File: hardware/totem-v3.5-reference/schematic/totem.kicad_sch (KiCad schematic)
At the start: 30 parts, among them J1 USB_C_Receptacle_USB2.0_16P, J2 LiPo 1000mAh, J3 u.FL GNSS, Q1 LED supply switch, SW1 power, SW2 SOS, U1 ESP32-WROOM-32E, U2 MAX-M10S, U4 AP2127K-3.3, U5 ICM-20948

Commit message: feat: footprints the library already knew, a title block, and the root sheet instance
Three things the documentation says a schematic should carry and this one
did not.

Footprints. Every one of the 85 placed instances had an empty Footprint
field — "each symbol in the schematic needs to have a footprint assigned to
it during the schematic entry process" (getting_started_in_kicad). Several
library symbols already name the package they are normally fitted in, and
that was being read and thrown away: the ESP32 module, the MAX-M10S, the
SOT-23-5 regulator, the ICM-20948's QFN and the WS2812B all arrive with one.
Eleven instances now carry a real footprint instead of a blank. The rest are
passives, connectors and switches, where the library cannot know and a
person has to choose.

A title block, which was empty. A sheet that says nothing about what it is
or how far to trust it is no good to anyone, and this one has to say both:
that it is a reconstruction rather than the Totem's recovered circuit, that
the passive values are designed to satisfy the firmware, that it is
generated and the source is what to edit, and that U3 is absent from the
drawing because no KiCad symbol for a TP4056 exists.

The root sheet_instances section, which the file format documentation lists
as a section of its own and which was simply missing.

Claude-Session: https://claude.ai/code/session_0192KwQN6XkBBxwoQn8x3FMV
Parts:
- DS1, DS61: footprint (none) -> LED_SMD:LED_WS2812B_PLCC4_5.0x5.0mm_P3.2mm
- U1: footprint (none) -> RF_Module:ESP32-WROOM-32E
- U2: footprint (none) -> RF_GPS:ublox_MAX
- U4: footprint (none) -> Package_TO_SOT_SMD:SOT-23-5
- U5: footprint (none) -> Sensor_Motion:InvenSense_QFN-24_3x3mm_P0.4mm
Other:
- company: (none) -> reconstruction, not the Totem's recovered circuit
- title: (none) -> Totem v3.5 — reference design

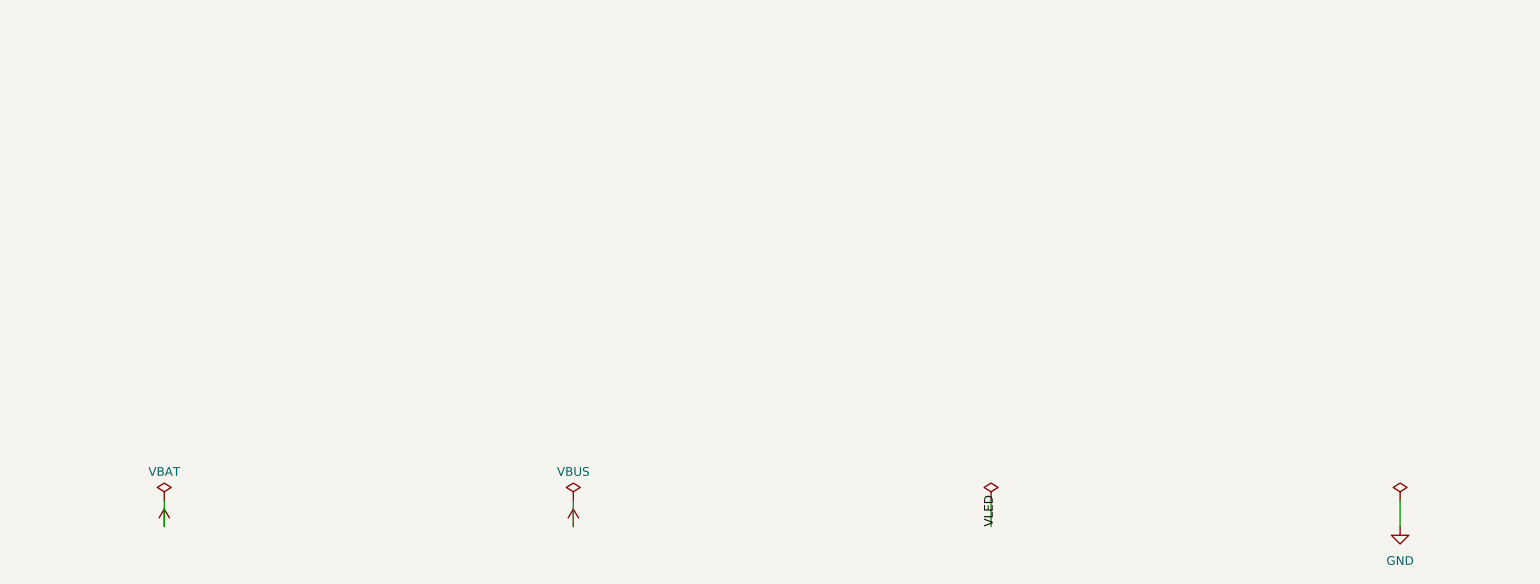
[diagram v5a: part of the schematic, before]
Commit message: fix: the charger was wired wrong, and the sheet was hiding it
I wrote "no KiCad symbol exists for the TP4056" and declared the part by
hand. Both halves were wrong. Battery_Management:TP4056-42-ESOP8 is in the
stock library, and the pinout I invented does not match the real part:

  pin 6  I called BAT2, "same die node as 5", and wired it to VBAT.
         It is STDBY, an open-drain status output.
  pin 8  I called STDBY and left it open.
         It is CE, the chip enable, and it is active high.

So the reference design shorted an open-drain output to the battery rail,
and never enabled the charger at all — CE floating means the part does
nothing. It would not have charged. Pin 6 is open now, CE is tied to the
input supply so charging runs whenever the cable is in, and pin 9, the
exposed thermal pad, goes to ground.

That the part was hand-declared is also why it was missing from the
drawing: a SKiDL-only part has no library, so it fell into `undrawn` and
the sheet quietly showed 30 of 31 components. The generator's own docstring
claimed it "cannot drift from the netlist"; this was the path that
falsified it. The sheet now has 31 symbols and the claim is true again.

Two things followed on their own. The VBAT PWR_FLAG is gone: the charger's
BAT pin is a real power output, so the rail has a genuine driver, and the
flag had been standing in for the missing part — quiet compensation that
hid the hole instead of showing it. And SKiDL's ERC went from two warnings
to none, so check.py's allowlist is empty, which is the honest state.

Verified by round trip, which is new and which would have caught this on
its own: KiCad exports a netlist back out of the drawing, and it now
carries the same 31 references as the netlist the circuit was built from,
with nothing on either side that is not on the other.

Claude-Session: https://claude.ai/code/session_0192KwQN6XkBBxwoQn8x3FMV
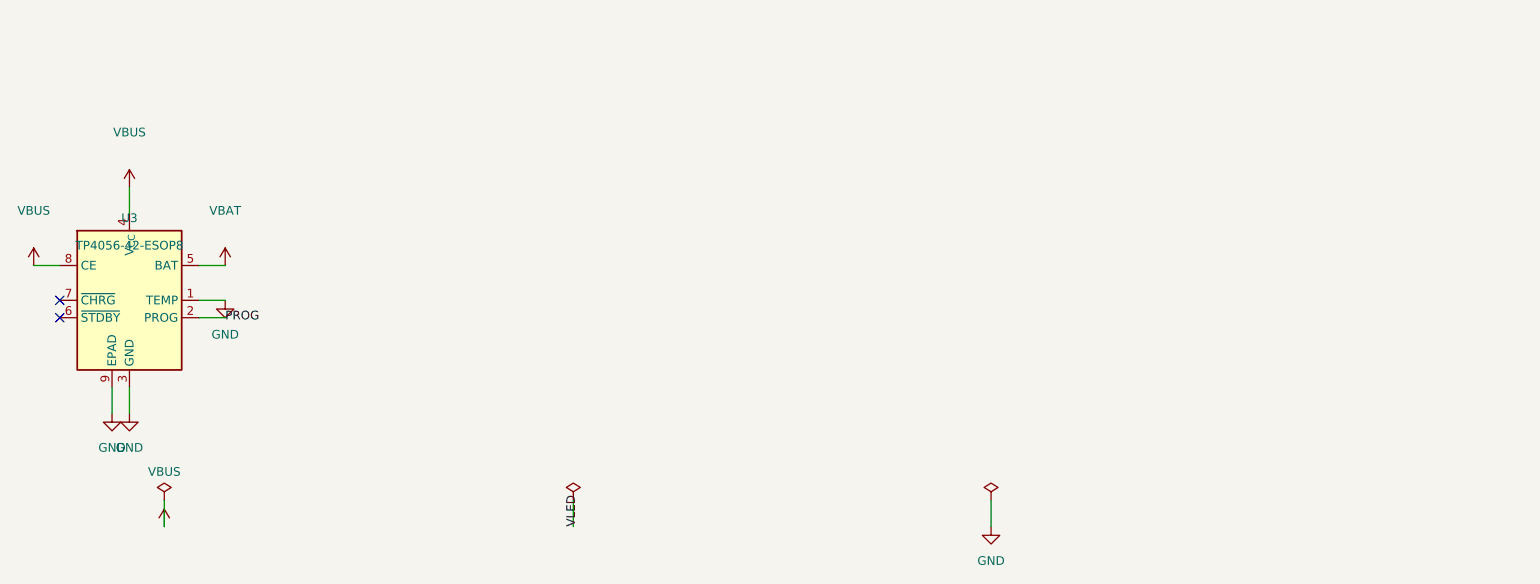
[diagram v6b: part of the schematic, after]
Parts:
- added U3: TP4056-42-ESOP8, Package_SO:SOIC-8-1EP_3.9x4.9mm_P1.27mm_EP2.41x3.3mm_ThermalVias, symbol Battery_Management:TP4056-42-ESOP8
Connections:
- net GND: now also U3.1 (TEMP), U3.3 (GND), U3.9 (EPAD)
- net PROG: now also U3.2 (PROG)
- net VBAT: now also U3.5 (BAT)
- net VBUS: now also U3.4 (V_{CC}), U3.8 (CE)
- no-connect marks 54 -> 56

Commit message: fix: a circuit that would work with the firmware, checked against the board
Reviewed against the photographs and the disassembly rather than against
the earlier reconstruction, and five things in it would not have worked.

The ring's power switch was inverted. LightStrip.power_on calls
pwr_gate.on(), so GPIO 19 goes HIGH to light the ring; a P-FET turns off
when its gate goes high, and the P-FET's gate was wired straight to GPIO 19.
The ring would have been dark exactly when the firmware asked for it. It
now has an N-FET in front of it (Q5), which is also what a P-FET marked
3401 on the board implies.

The ring LEDs could not have been placed. Sixty pixels around a ~40 mm
circle leaves about 2 mm each, so they are WS2812B-2020, not the 5 x 5 mm
WS2812B the footprint had. The 2020 also has a different pinout.

The crystal would have flattened the cell while switched off. The firmware
gates only the ring; the crystal has no power gate. On the cell directly,
seven dark WS2812Bs draw about 5 mA forever, which empties a 1000 mAh cell
in roughly eight days with the device off. Everything now sits behind a
main switch (VSYS), so off really is off.

The power latch put 4.2 V on GPIO 4. The button raised the regulator's
enable to the cell voltage and that reached GPIO 4 through a resistor,
above the ESP32's 3.6 V maximum, and made presses unreadable. The new latch
satisfies each thing the firmware requires of GPIO 4: a press turns the
board on, it stays on, the pin reads the button low with the pull-up, a
firmware low turns the board off, and a press while running does not,
because the button itself holds the latch while it is down.

A USB-C charger would have supplied nothing. CC1 and CC2 need 5.1k to
ground before a source turns VBUS on; they were not connected.

Also added because a real board needs them: decoupling on every supply,
Espressif's 10k/1uF reset, programming pads for UART0 and the boot strap
(the USB-C carries no data, so without them a bare board cannot be
f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
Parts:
- removed DS1: halo, 60 px, LED_SMD:LED_WS2812B_PLCC4_5.0x5.0mm_P3.2mm, symbol LED:WS2812B
- removed DS61: crystal, 7 px, LED_SMD:LED_WS2812B_PLCC4_5.0x5.0mm_P3.2mm, symbol LED:WS2812B
- removed DS68: SOS, symbol Device:LED
- added C10, C11, C13, C14, C15, C16, C17, C3, C5: 10u, Capacitor_SMD:C_0603_1608Metric, symbol Device:C
- added C12, C4, C6, C7, C8: 100n, Capacitor_SMD:C_0402_1005Metric, symbol Device:C
- added C18: 1u, Capacitor_SMD:C_0402_1005Metric, symbol Device:C
- added D1: 1N4148W, Diode_SMD:D_SOD-123, symbol Diode:1N4148W
- added D100, D101, D102, D103, D104, D105, D106, D107, D108, D109, D110, D111, D112, D113, D114, D115, D116, D117, D118, D119, D120, D121, D122, D123, D124, D125, D126, D127, D128, D129, D130, D131, D132, D133, D134, D135, D136, D137, D138, D139, D140, D141, D142, D143, D144, D145, D146, D147, D148, D149, D150, D151, D152, D153, D154, D155, D156, D157, D158, D159, D200, D201, D202, D203, D204, D205, D206: WS2812B-2020, LED_SMD:LED_WS2812B-2020_PLCC4_2.0x2.0mm, symbol LED:WS2812B-2020
- added D2: BAT54W, Package_TO_SOT_SMD:SOT-323_SC-70, symbol Diode:BAT54W
- added D3: red, LED_SMD:LED_0603_1608Metric, symbol Device:LED
- added Q2, Q3, Q5: 2N7002, Package_TO_SOT_SMD:SOT-23, symbol Transistor_FET:2N7002
- added Q4: AO3401A, Package_TO_SOT_SMD:SOT-23, symbol Transistor_FET:AO3401A
- added R14, R18, R24, R25: 100k, Resistor_SMD:R_0402_1005Metric, symbol Device:R
- added R15: 10M, Resistor_SMD:R_0402_1005Metric, symbol Device:R
- added R16: 1M, Resistor_SMD:R_0402_1005Metric, symbol Device:R
- added R17, R19, R22, R26: 10k, Resistor_SMD:R_0402_1005Metric, symbol Device:R
- added R20, R21: 5.1k, Resistor_SMD:R_0402_1005Metric, symbol Device:R
- added R23: 2.2k, Resistor_SMD:R_0402_1005Metric, symbol Device:R
- added TP2: 3V3, TestPoint:TestPoint_Pad_D1.0mm, symbol Connector:TestPoint
- added TP3: GND, TestPoint:TestPoint_Pad_D1.0mm, symbol Connector:TestPoint
- added TP4: TXD0, TestPoint:TestPoint_Pad_D1.0mm, symbol Connector:TestPoint
- added TP5: RXD0, TestPoint:TestPoint_Pad_D1.0mm, symbol Connector:TestPoint
- added TP6: EN, TestPoint:TestPoint_Pad_D1.0mm, symbol Connector:TestPoint
- added TP7: IO0, TestPoint:TestPoint_Pad_D1.0mm, symbol Connector:TestPoint
- C1: footprint (none) -> Capacitor_SMD:C_0402_1005Metric
- C2: value 100n -> 1u; footprint (none) -> Capacitor_SMD:C_0402_1005Metric
- J1: footprint (none) -> Connector_USB:USB_C_Receptacle_HRO_TYPE-C-31-M-12
- J2: footprint (none) -> Connector_JST:JST_PH_S2B-PH-SM4-TB_1x02-1MP_P2.00mm_Horizontal
- J3: value u.FL GNSS -> u.FL; footprint (none) -> Connector_Coaxial:U.FL_Hirose_U.FL-R-SMT-1_Vertical; symbol Connector_Generic:Conn_01x01 -> Connector:Conn_Coaxial
- MK1: value MEMS -> electret; footprint (none) -> Sensor_Audio:CUI_CMC-4013-SMT; symbol Device:Microphone -> Device:Microphone_Condenser
- Q1: value LED supply switch -> AO3401A; footprint (none) -> Package_TO_SOT_SMD:SOT-23; symbol Device:Q_PMOS -> Transistor_FET:AO3401A
- R1, R10, R13, R2, R3, R4, R9: footprint (none) -> Resistor_SMD:R_0402_1005Metric
- R11: value 10k -> 33; footprint (none) -> Resistor_SMD:R_0402_1005Metric
- R12: value 2k2 -> 33; footprint (none) -> Resistor_SMD:R_0402_1005Metric
- R5: value 1k2 -> 2k; footprint (none) -> Resistor_SMD:R_0402_1005Metric
- R6: value 330R -> 330; footprint (none) -> Resistor_SMD:R_0402_1005Metric
- R7, R8: value 4k7 -> 4.7k; footprint (none) -> Resistor_SMD:R_0402_1005Metric
- SW1, SW2: footprint (none) -> totem:SW_Side_6x6
- TP1: value touch pad -> touch; footprint (none) -> TestPoint:TestPoint_THTPad_D2.0mm_Drill1.0mm; symbol Connector_Generic:Conn_01x01 -> Connector:TestPoint
- U3: footprint Package_SO:SOIC-8-1EP_3.9x4.9mm_P1.27mm_EP2.41x3.3mm_ThermalVias -> Package_SO:SOIC-8-1EP_3.9x4.9mm_P1.27mm_EP2.29x3mm
- U4: value AP2127K-3.3 -> AP2112K-3.3; symbol Regulator_Linear:AP2127K-3.3 -> Regulator_Linear:AP2112K-3.3
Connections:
- net +3V3: now also C14.1, C3.1, C4.1, C5.1, C6.1, C7.1, C8.1, R16.1, R19.1, R22.1, R23.1, R24.1, TP2.1; no longer R12.1
- net BTN_SOS: now also R22.2, TP7.1
- net CRYSTAL_DATA: now also R12.1
- net ESP_EN: now also TP6.1
- net GND: now also J3.2 (Ext), C10.2, C11.2, C12.2, C13.2, C14.2, C15.2, C16.2, C17.2, C3.2, C4.2, C5.2, C6.2, C7.2, C8.2, D100.2 (VSS), D101.2 (VSS), D102.2 (VSS), D103.2 (VSS), D104.2 (VSS), D105.2 (VSS), D106.2 (VSS), D107.2 (VSS), D108.2 (VSS), D109.2 (VSS), D110.2 (VSS), D111.2 (VSS), D112.2 (VSS), D113.2 (VSS), D114.2 (VSS), D115.2 (VSS), D116.2 (VSS), D117.2 (VSS), D118.2 (VSS), D119.2 (VSS), D120.2 (VSS), D121.2 (VSS), D122.2 (VSS), D123.2 (VSS), D124.2 (VSS), D125.2 (VSS), D126.2 (VSS), D127.2 (VSS), D128.2 (VSS), D129.2 (VSS), D130.2 (VSS), D131.2 (VSS), D132.2 (VSS), D133.2 (VSS), D134.2 (VSS), D135.2 (VSS), D136.2 (VSS), D137.2 (VSS), D138.2 (VSS), D139.2 (VSS), D140.2 (VSS), D141.2 (VSS), D142.2 (VSS), D143.2 (VSS), D144.2 (VSS), D145.2 (VSS), D146.2 (VSS), D147.2 (VSS), D148.2 (VSS), D149.2 (VSS), D150.2 (VSS), D151.2 (VSS), D152.2 (VSS), D153.2 (VSS), D154.2 (VSS), D155.2 (VSS), D156.2 (VSS), D157.2 (VSS), D158.2 (VSS), D159.2 (VSS), D200.2 (VSS), D201.2 (VSS), D202.2 (VSS), D203.2 (VSS), D204.2 (VSS), D205.2 (VSS), D206.2 (VSS), D3.1 (K), Q2.2 (S), Q3.2 (S), Q5.2 (S), R15.2, R18.2, R20.2, R21.2, R25.2, R26.2, TP3.1; no longer U5.9 (SDO/AD0)
- net GPIO4: now also D2.3 (K), Q3.3 (D), R19.2; no longer R11.2
- net LED_EN: now also R10.1, Q5.1 (G); no longer Q1.G, R9.2
- net MIC: now also C18.2, R24.2, R25.1; no longer MK1.2 (+), R12.2
- net RING_DATA: now also R11.1
- net SOS_LED_A: now also D3.2 (A)
- net VBAT: now also Q1.2 (S), SW1.1, C11.1, R14.1; no longer Q1.S, R1.1, R9.1, SW1.2, U4.1 (VIN)
- net VBUS: now also C10.1
- net VLED: now also C15.1, C16.1, D100.4 (VDD), D101.4 (VDD), D102.4 (VDD), D103.4 (VDD), D104.4 (VDD), D105.4 (VDD), D106.4 (VDD), D107.4 (VDD), D108.4 (VDD), D109.4 (VDD), D110.4 (VDD), D111.4 (VDD), D112.4 (VDD), D113.4 (VDD), D114.4 (VDD), D115.4 (VDD), D116.4 (VDD), D117.4 (VDD), D118.4 (VDD), D119.4 (VDD), D120.4 (VDD), D121.4 (VDD), D122.4 (VDD), D123.4 (VDD), D124.4 (VDD), D125.4 (VDD), D126.4 (VDD), D127.4 (VDD), D128.4 (VDD), D129.4 (VDD), D130.4 (VDD), D131.4 (VDD), D132.4 (VDD), D133.4 (VDD), D134.4 (VDD), D135.4 (VDD), D136.4 (VDD), D137.4 (VDD), D138.4 (VDD), D139.4 (VDD), D140.4 (VDD), D141.4 (VDD), D142.4 (VDD), D143.4 (VDD), D144.4 (VDD), D145.4 (VDD), D146.4 (VDD), D147.4 (VDD), D148.4 (VDD), D149.4 (VDD), D150.4 (VDD), D151.4 (VDD), D152.4 (VDD), D153.4 (VDD), D154.4 (VDD), D155.4 (VDD), D156.4 (VDD), D157.4 (VDD), D158.4 (VDD), D159.4 (VDD), Q4.3 (D); no longer Q1.D
- net RXD0: now reaches U1.34 (RXD0/IO3)
- net RXD0: now also TP5.1
- net TXD0: now reaches U1.35 (TXD0/IO1)
- net TXD0: now also TP4.1
- net CC1: now reaches J1.A5 (CC1)
- net CC1: now also R20.1
- net CC2: now reaches J1.B5 (CC2)
- net CC2: now also R21.1
- net N$1 renamed REGOUT
- removed net POWER_EN: R10.1, R11.1, SW1.1, U4.3 (EN)
- new net: D122.1 (DOUT), D123.3 (DIN)
- new net: D121.1 (DOUT), D122.3 (DIN)
- new net: D205.1 (DOUT), D206.3 (DIN)
- new net: D204.1 (DOUT), D205.3 (DIN)
- new net: D201.1 (DOUT), D202.3 (DIN)
- new net: D200.1 (DOUT), D201.3 (DIN)
- new net: D140.1 (DOUT), D141.3 (DIN)
- new net: D100.1 (DOUT), D101.3 (DIN)
- new net: D123.1 (DOUT), D124.3 (DIN)
- new net: D134.1 (DOUT), D135.3 (DIN)
- new net: D133.1 (DOUT), D134.3 (DIN)
- new net: D142.1 (DOUT), D143.3 (DIN)
- new net: D141.1 (DOUT), D142.3 (DIN)
- new net: D158.1 (DOUT), D159.3 (DIN)
- new net: D131.1 (DOUT), D132.3 (DIN)
- new net: D130.1 (DOUT), D131.3 (DIN)
- new net: D104.1 (DOUT), D105.3 (DIN)
- new net: D103.1 (DOUT), D104.3 (DIN)
- new net: D118.1 (DOUT), D119.3 (DIN)
- new net: D132.1 (DOUT), D133.3 (DIN)
- new net: D120.1 (DOUT), D121.3 (DIN)
- new net: D136.1 (DOUT), D137.3 (DIN)
- new net: D135.1 (DOUT), D136.3 (DIN)
- new net: D112.1 (DOUT), D113.3 (DIN)
- new net: D111.1 (DOUT), D112.3 (DIN)
- new net: D117.1 (DOUT), D118.3 (DIN)
- new net: D116.1 (DOUT), D117.3 (DIN)
- new net: D143.1 (DOUT), D144.3 (DIN)
- new net: D149.1 (DOUT), D150.3 (DIN)
- new net: D148.1 (DOUT), D149.3 (DIN)
- new net: D138.1 (DOUT), D139.3 (DIN)
- new net: D137.1 (DOUT), D138.3 (DIN)
- new net: D154.1 (DOUT), D155.3 (DIN)
- new net: D153.1 (DOUT), D154.3 (DIN)
- new net: D152.1 (DOUT), D153.3 (DIN)
- new net: D151.1 (DOUT), D152.3 (DIN)
- new net: D109.1 (DOUT), D110.3 (DIN)
- new net: D108.1 (DOUT), D109.3 (DIN)
- new net: D124.1 (DOUT), D125.3 (DIN)
- new net: D129.1 (DOUT), D130.3 (DIN)
- new net: D128.1 (DOUT), D129.3 (DIN)
- new net: D145.1 (DOUT), D146.3 (DIN)
- new net: D144.1 (DOUT), D145.3 (DIN)
- new net: D115.1 (DOUT), D116.3 (DIN)
- new net: D114.1 (DOUT), D115.3 (DIN)
- new net: D147.1 (DOUT), D148.3 (DIN)
- new net: D107.1 (DOUT), D108.3 (DIN)
- new net: D106.1 (DOUT), D107.3 (DIN)
- new net: D113.1 (DOUT), D114.3 (DIN)
- new net: D126.1 (DOUT), D127.3 (DIN)
- new net: D125.1 (DOUT), D126.3 (DIN)
- new net: D203.1 (DOUT), D204.3 (DIN)
- new net: D157.1 (DOUT), D158.3 (DIN)
- new net: D105.1 (DOUT), D106.3 (DIN)
- new net: D110.1 (DOUT), D111.3 (DIN)
- new net: D102.1 (DOUT), D103.3 (DIN)
- new net: D101.1 (DOUT), D102.3 (DIN)
- new net: D2.1 (A), R17.2
- new net: D156.1 (DOUT), D157.3 (DIN)
- new net: D150.1 (DOUT), D151.3 (DIN)
- new net: D202.1 (DOUT), D203.3 (DIN)
- new net: D127.1 (DOUT), D128.3 (DIN)
- new net: D146.1 (DOUT), D147.3 (DIN)
- new net: D155.1 (DOUT), D156.3 (DIN)
- new net BTN: D1.2 (A), Q3.1 (G), R18.1, SW1.2
- new net CRY_D0: D200.3 (DIN), R12.2
- new net GATE_MAIN: Q1.1 (G), Q2.3 (D), R14.2
- new net HOLD: C12.1, D1.1 (K), Q2.1 (G), R15.1, R16.2, R17.1
- new net IMU_AD0: R26.1, U5.9 (SDO/AD0)
- new net MIC_RAW: C18.1, MK1.2 (+), R23.2
- new net RING_D0: D100.3 (DIN), R11.2
- new net RING_D20: D119.1 (DOUT), D120.3 (DIN)
- new net RING_D40: D139.1 (DOUT), D140.3 (DIN)
- new net RING_GATE: Q4.1 (G), Q5.3 (D), R9.2
- new net VSYS: C13.1, C17.1, D200.4 (VDD), D201.4 (VDD), D202.4 (VDD), D203.4 (VDD), D204.4 (VDD), D205.4 (VDD), D206.4 (VDD), Q1.3 (D), Q4.2 (S), R1.1, R9.1, U4.1 (VIN), U4.3 (EN)
- no-connect marks 56 -> 53
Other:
- moved on the sheet: C1, C2, J1, J2, R1, R10, R11, R12, R13, R2, R3, R4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
